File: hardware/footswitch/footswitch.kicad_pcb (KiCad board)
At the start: 2 copper layers, 34 x 24 mm, 4 parts, among them J1 Conn_02x05_Counter_Clockwise

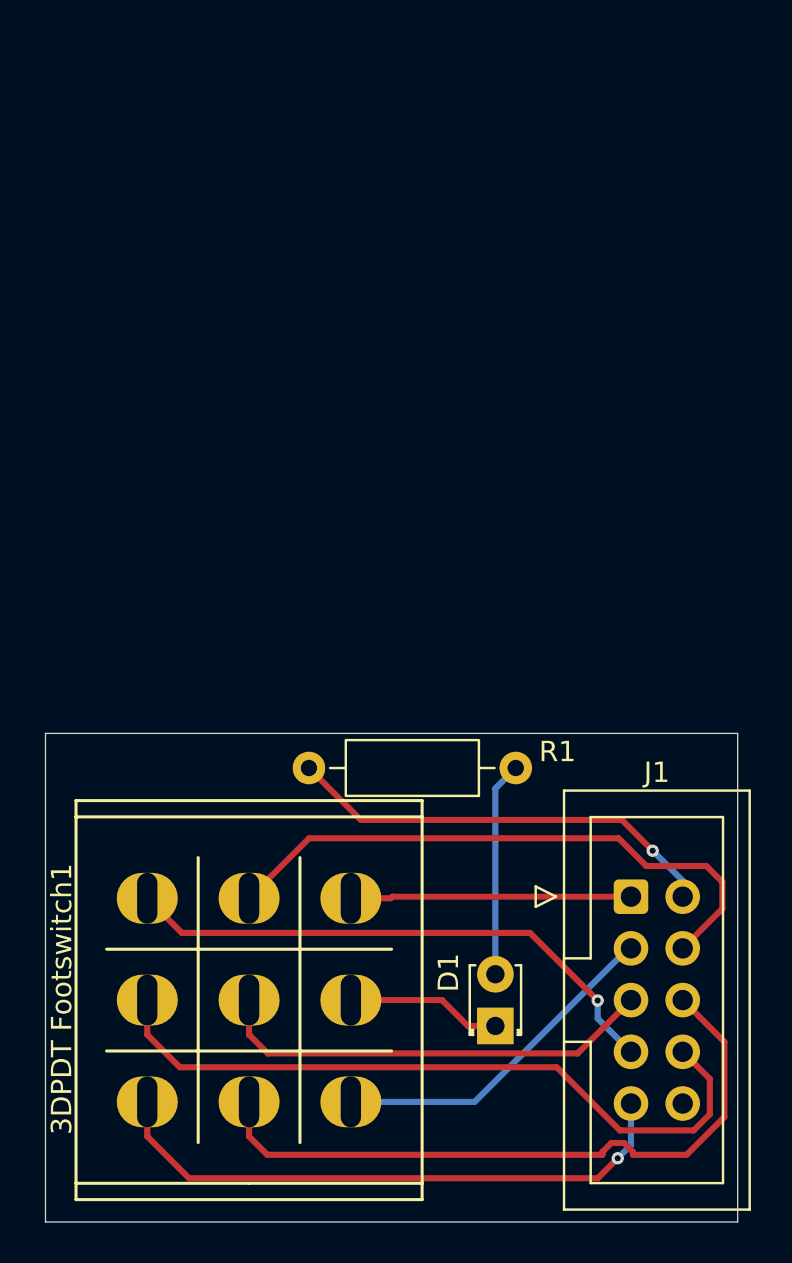
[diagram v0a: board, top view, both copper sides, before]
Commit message: Adapt board for pcb mounted footswitches
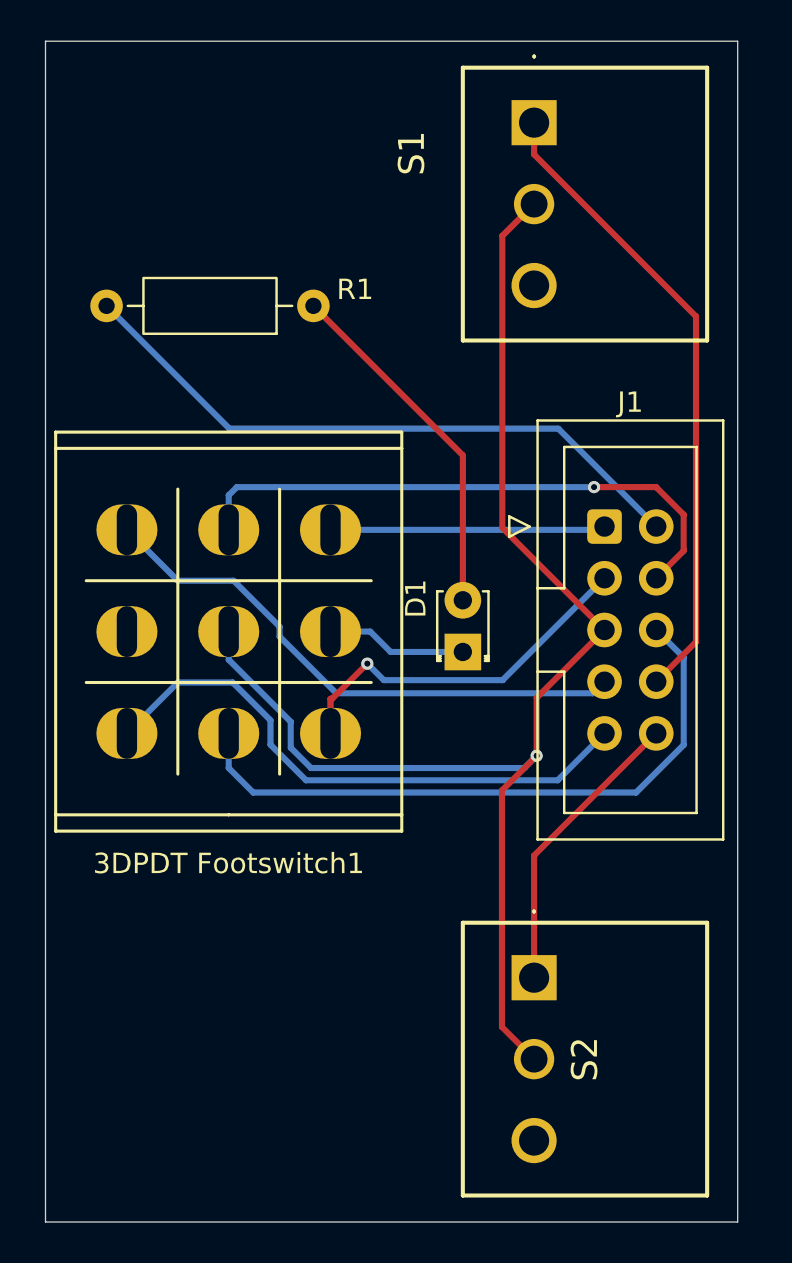
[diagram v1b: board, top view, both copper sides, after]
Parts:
- added S1: SF12011F-0102-20R-M-050, pcb switch:SF12011F010220RM050, F.Cu at (154.0, 69.0)
- added S2: SF12011F-0102-20R-M-050, pcb switch:SF12011F010220RM050, F.Cu at (154.0, 111.0)
- moved R1 24.8 mm to (143.2, 78.0)
- moved D1 18.4 mm to (150.5, 95.0)
- moved J1 18.2 mm to (157.5, 88.8)
- moved 3DPDT Footswitch1 18.1 mm to (139.0, 94.0)
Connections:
- 3DPDT Footswitch1 pad 8: /conn8 -> unconnected-(3DPDT Footswitch1-G-Pad8)
- J1 pad 10: unconnected-(J1-Pin_10-Pad10) -> /conn10
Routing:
- net /conn5: track 21.9 -> 67.2 mm, vias 0 -> 1
- net /conn10: track 0.00 -> 14.5 mm
- net /conn2: track 21.4 -> 31.5 mm, vias 1 -> 0
- net Net-(D1-A): track 10.5 -> 17.5 mm
- net /conn8: track 35.2 -> 31.6 mm
- net /conn3: track 16.9 -> 18.8 mm, vias 0 -> 1
- net /conn6: track 33.4 -> 31.7 mm
- net /conn4: track 29.4 -> 28.5 mm, vias 0 -> 1
- net /conn9: track 29.0 -> 28.1 mm, vias 1 -> 0
- net /fsw2: track 7.63 -> 6.91 mm
- net /conn7: track 27.4 -> 27.3 mm, vias 1 -> 0
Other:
- board size 34 x 24 mm -> 34 x 58 mm
